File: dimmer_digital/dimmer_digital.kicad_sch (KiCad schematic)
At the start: 31 parts, among them J1 Conn_01x04_Pin, Q1 BC558, Q2 BC558, Q3 BT139-600, U1 ATmega328P-P, U2 MAX232, U3 74LS47, U4 4N25, U5 MOC3021M, U6 D168K, U7 D168K, U8 4N25

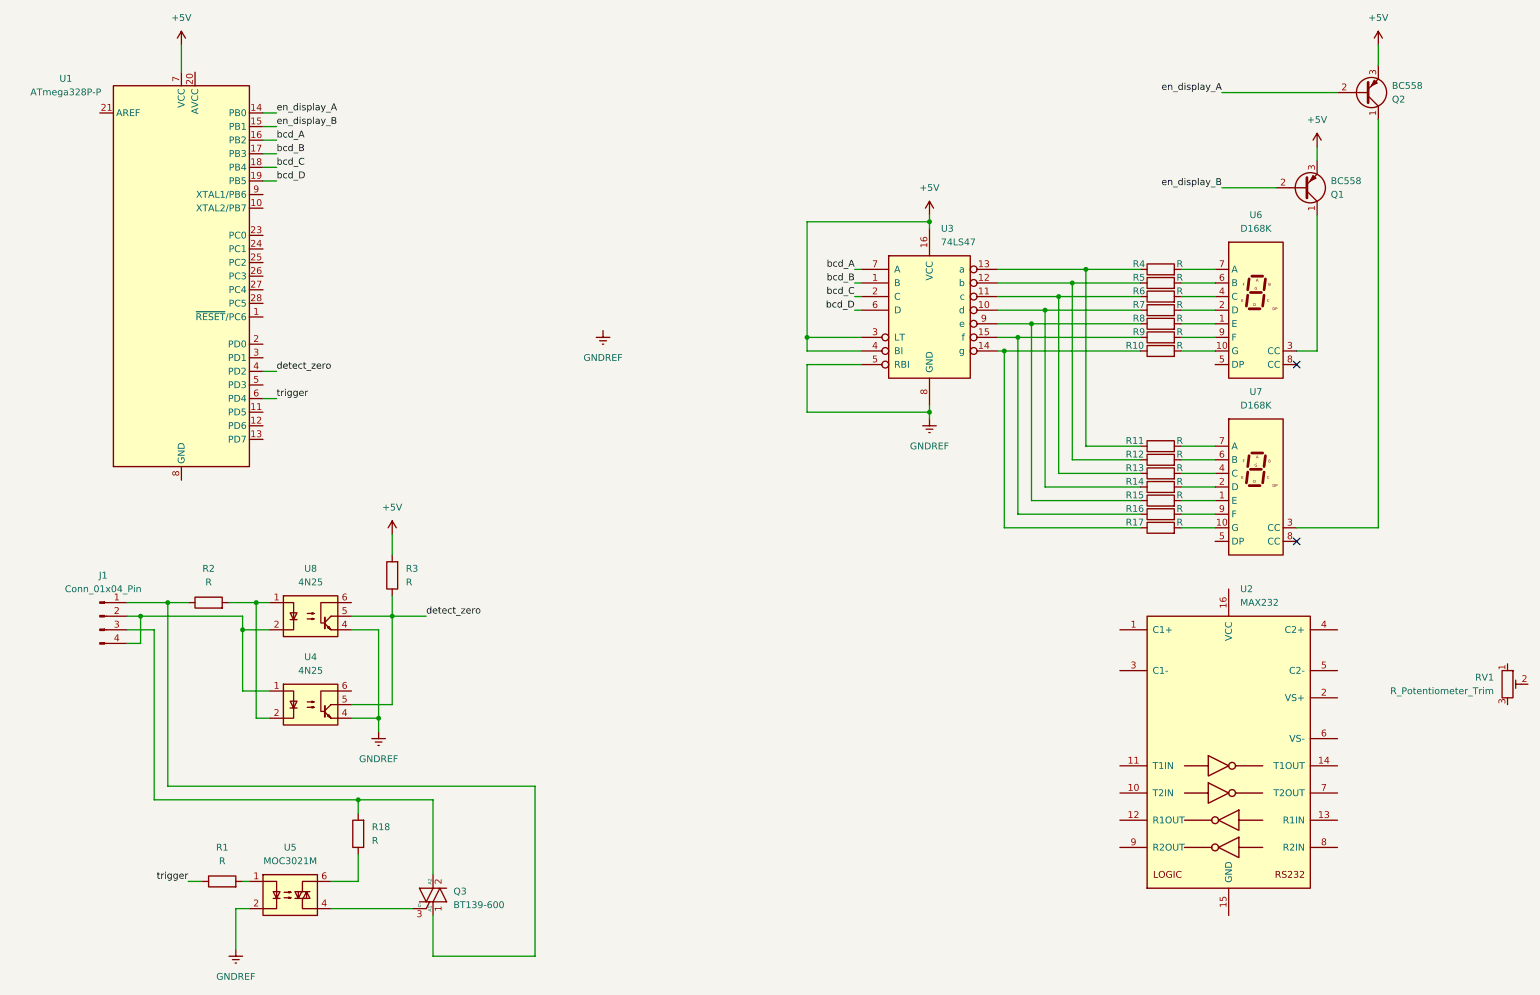
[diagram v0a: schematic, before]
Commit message: Put the values in resistors
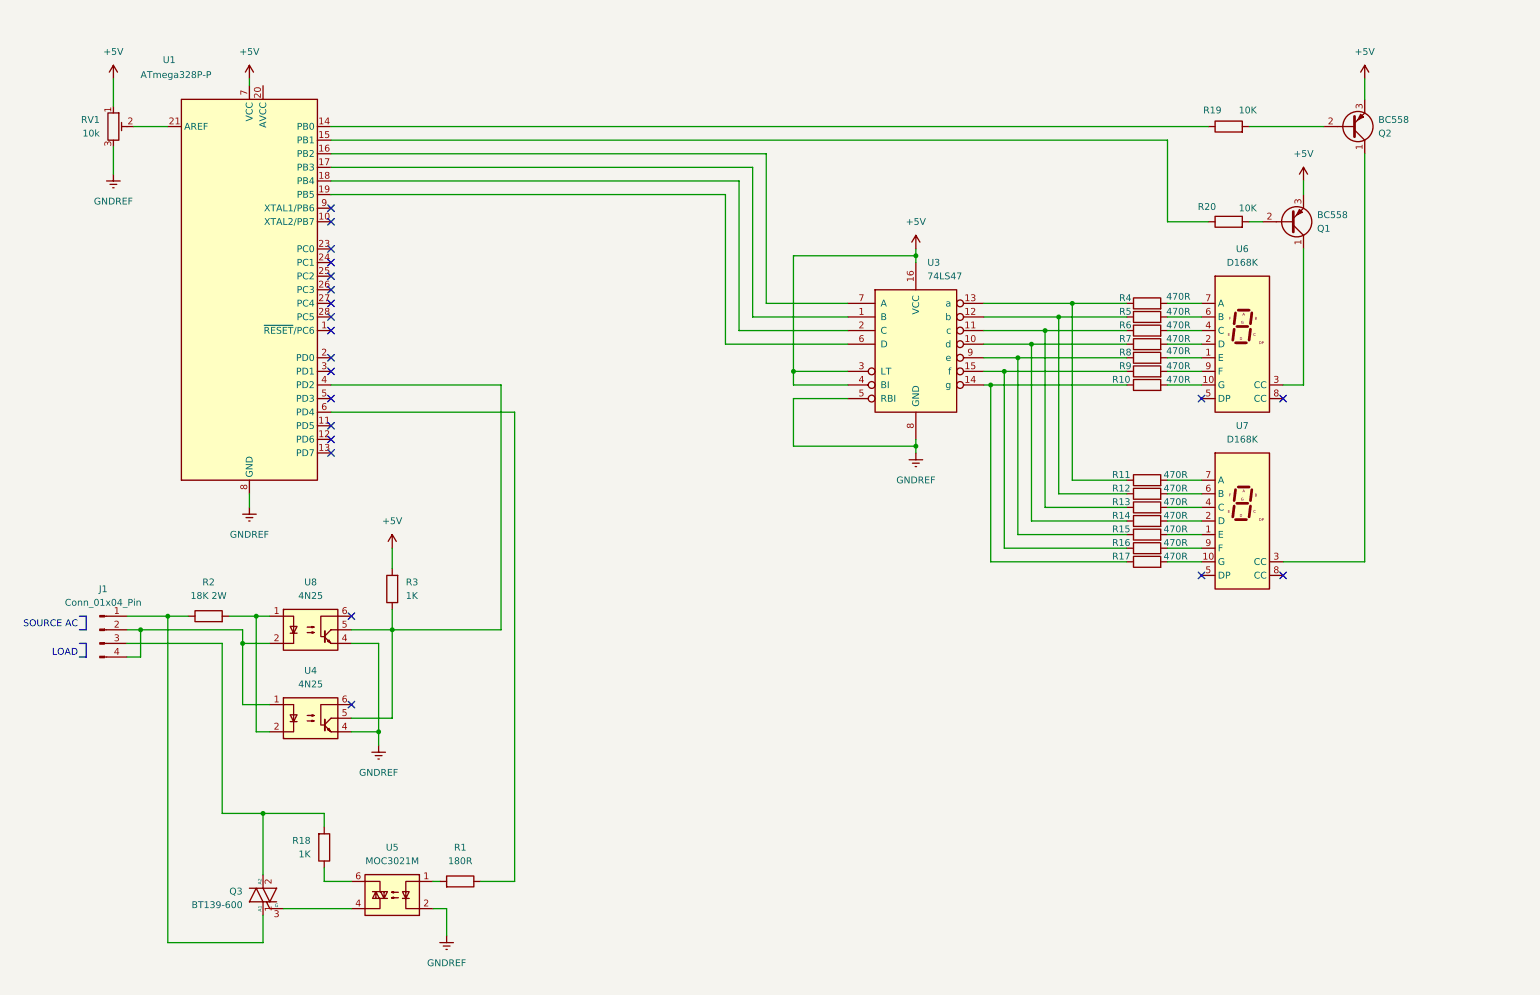
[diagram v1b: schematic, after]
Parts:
- removed U2: MAX232, symbol Interface_UART:MAX232
- added R19, R20: 10K, symbol Device:R
- R1: value R -> 180R
- R10, R11, R12, R13, R14, R15, R16, R17, R4, R5, R6, R7, R8, R9: value R -> 470R
- R18, R3: value R -> 1K
- R2: value R -> 18K 2W
- RV1: value R_Potentiometer_Trim -> 10k
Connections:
- net +5V: now also RV1.1
- net GNDREF: now also RV1.3, U1.22 (GND), U1.8 (GND)
- net at RV1.2: now also U1.21 (AREF)
- net bcd_A: no longer names the net of U1.16 (PB2), U3.7 (A)
- net bcd_B: no longer names the net of U1.17 (PB3), U3.1 (B)
- net bcd_C: no longer names the net of U1.18 (PB4), U3.2 (C)
- net bcd_D: no longer names the net of U1.19 (PB5), U3.6 (D)
- net detect_zero: no longer names the net of R3.1, U1.4 (PD2), U4.5, U8.5
- net en_display_A: no longer names the net of U1.14 (PB0)
- net en_display_A: now also R19.1; no longer Q2.2 (B)
- net en_display_B: no longer names the net of U1.15 (PB1)
- net en_display_B: now also R20.1; no longer Q1.2 (B)
- net trigger: no longer names the net of R1.1, U1.6 (PD4)
- new net: Q1.2 (B), R20.2
- new net: Q2.2 (B), R19.2
- no-connect marks 2 -> 21
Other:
- note added: "LOAD"
- note added: "SOURCE AC"
- moved on the sheet: J1, Q1, Q2, Q3, R1, R10, R11, R12, R13, R14, R15, R16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
